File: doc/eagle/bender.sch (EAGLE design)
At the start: 11 parts

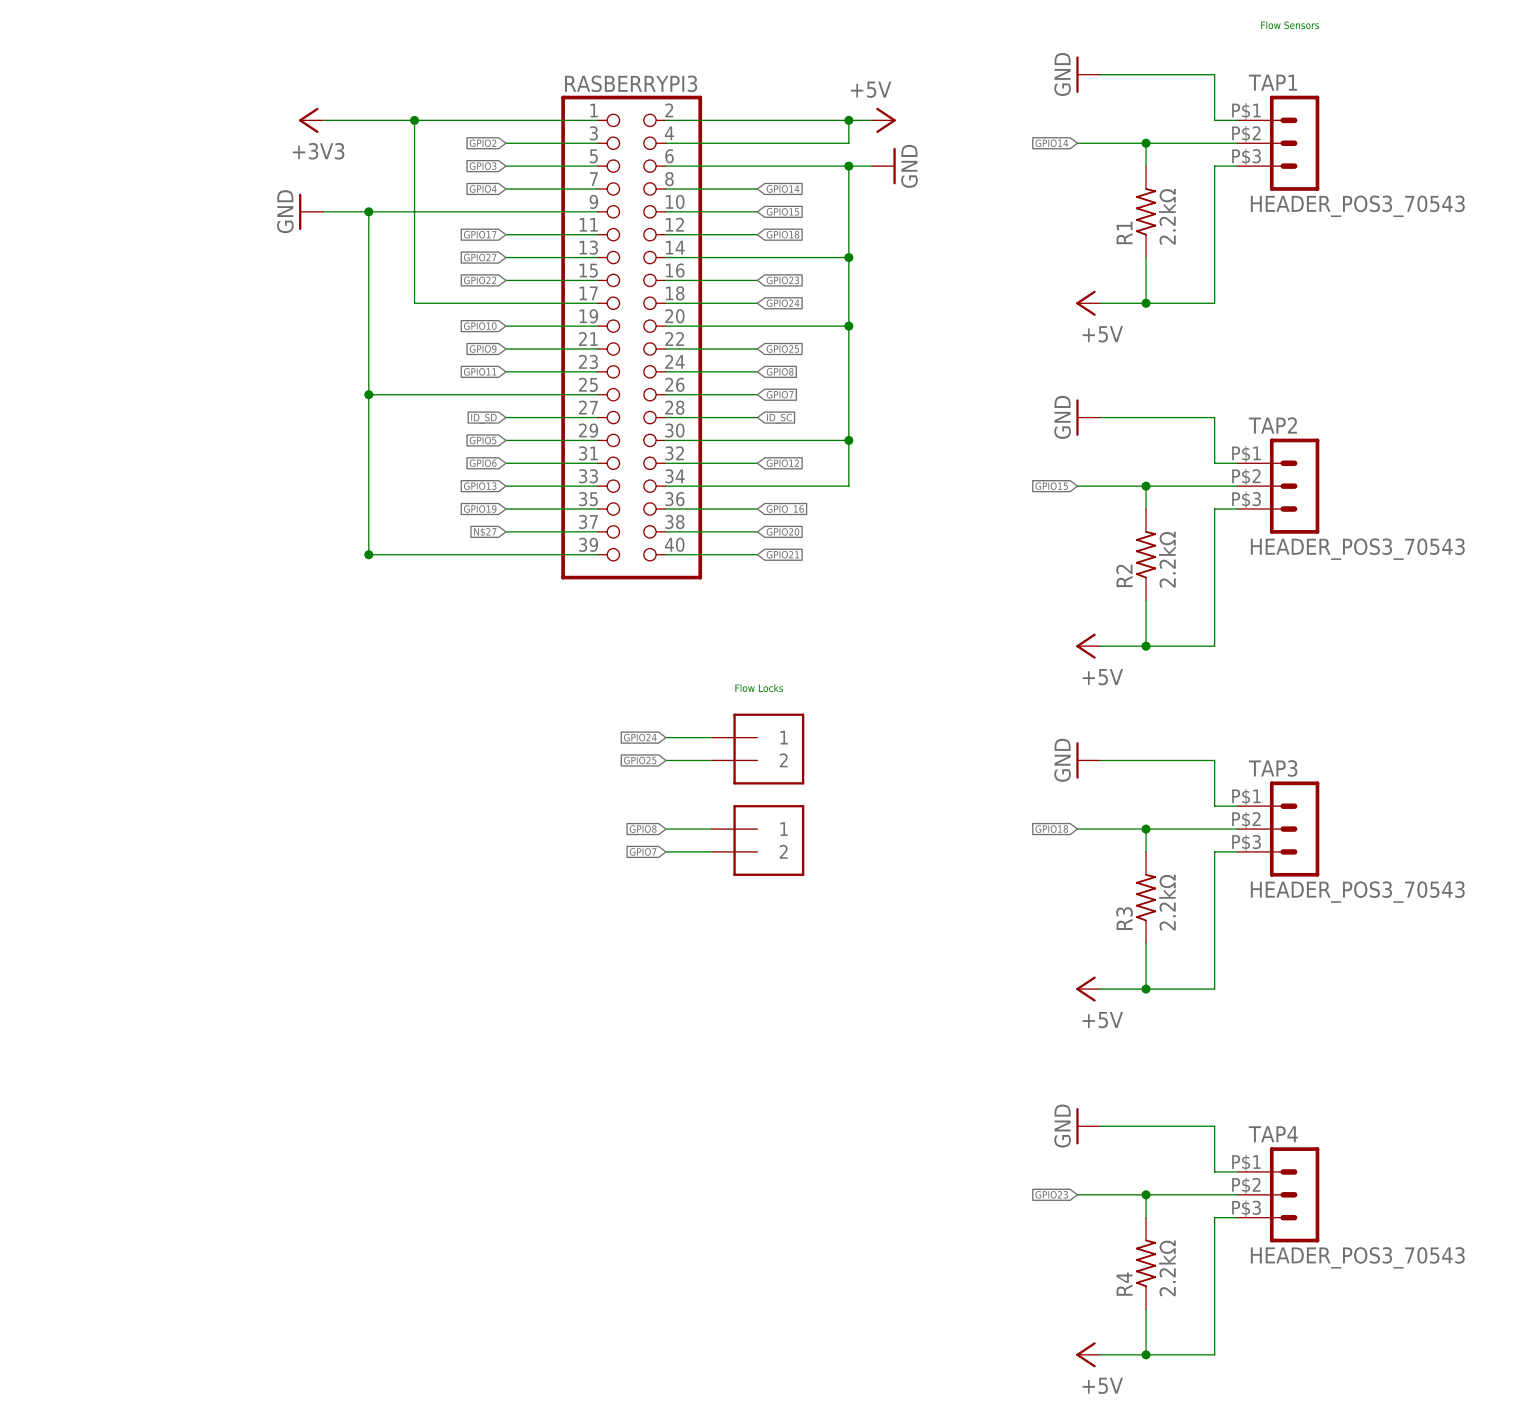
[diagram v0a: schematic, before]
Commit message: Update schematics to use 3v3 for Pi inputs.
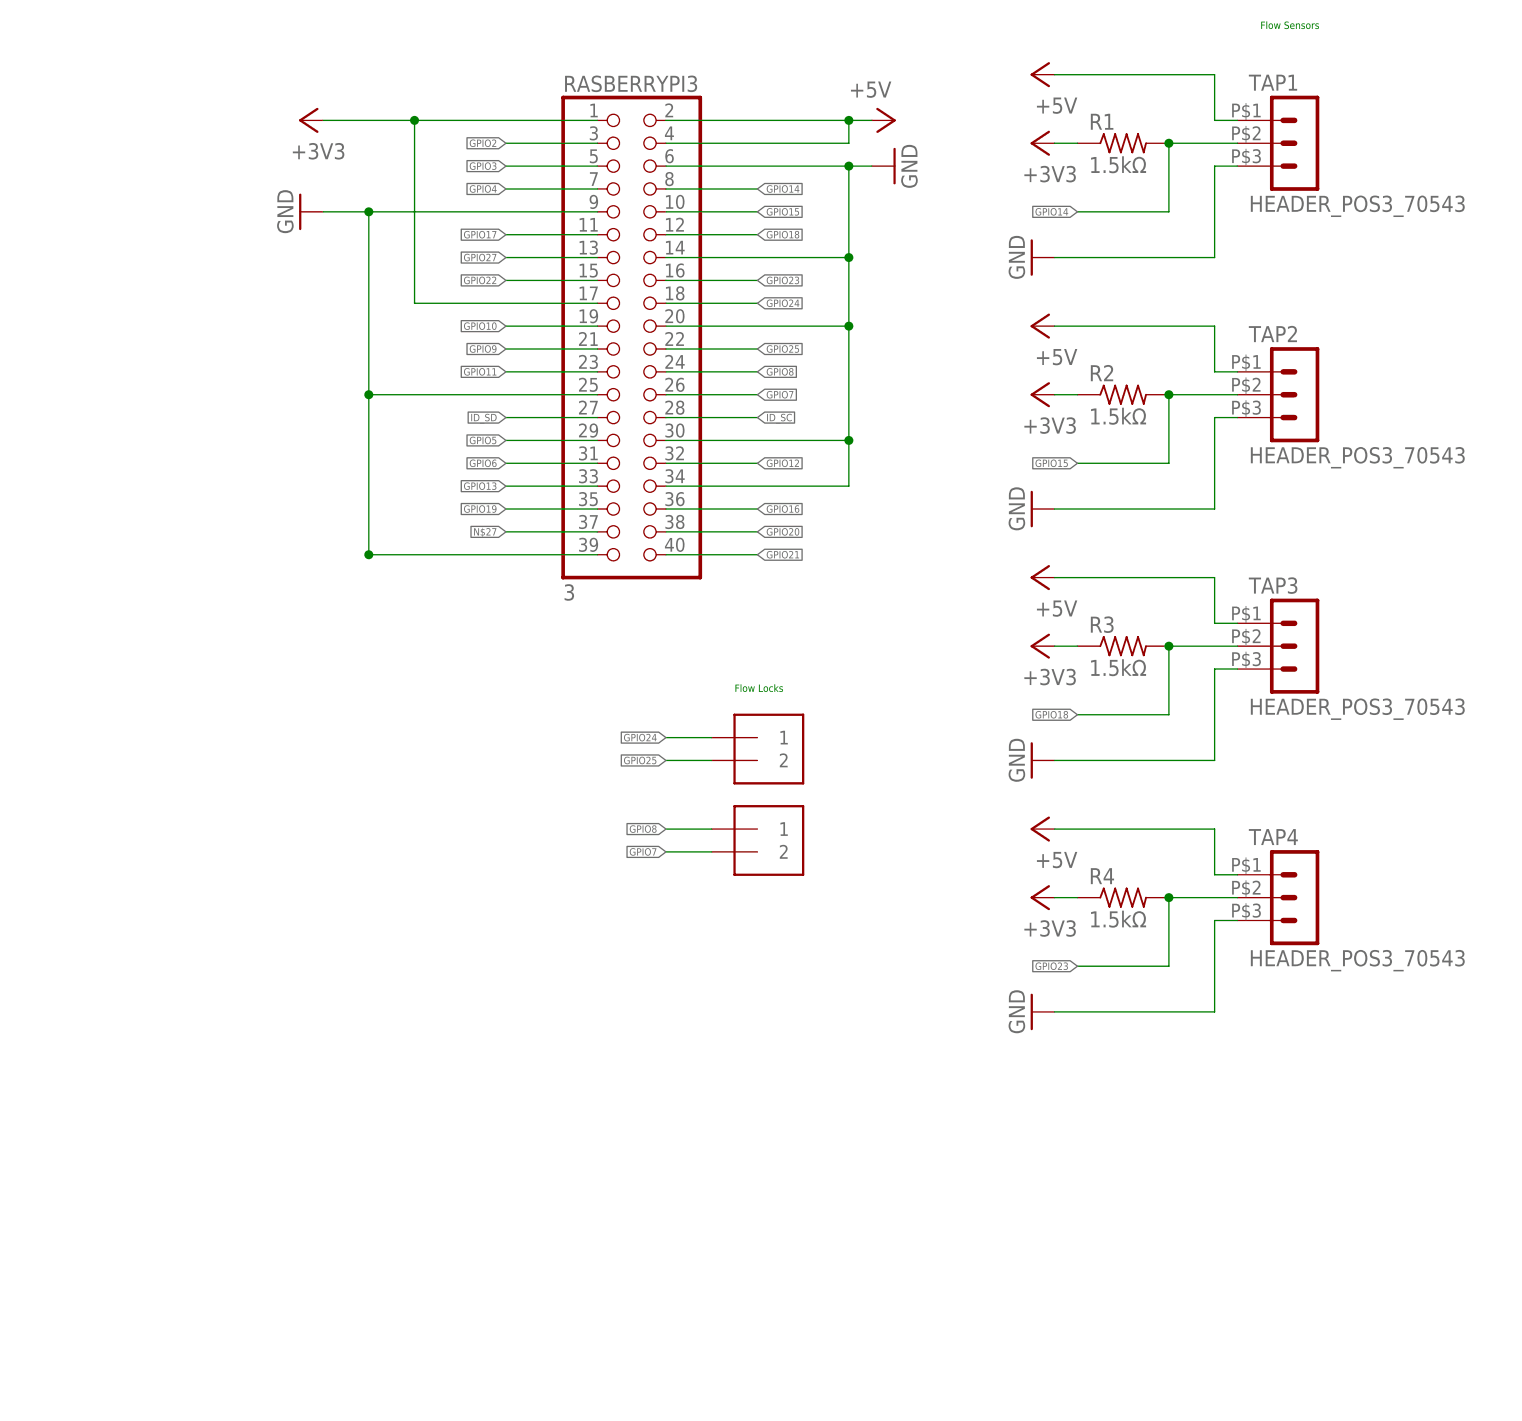
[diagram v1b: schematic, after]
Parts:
- R1, R2, R3, R4: value 2.2kΩ -> 1.5kΩ
- RASBERRYPI3: value (none) -> 3
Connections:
- net GPIO_16 renamed GPIO16
- net +3V3: now also R1.1, R2.1, R3.1, R4.1
- net +5V: now also TAP1.1, TAP2.1, TAP3.1, TAP4.1; no longer R1.1, R2.1, R3.1, R4.1, TAP1.3, TAP2.3, TAP3.3, TAP4.3
- net GND: now also TAP1.3, TAP2.3, TAP3.3, TAP4.3; no longer TAP1.1, TAP2.1, TAP3.1, TAP4.1
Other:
- moved on the sheet: R1, R2, R3, R4, TAP2, TAP3, TAP4

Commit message: Add temp sensor to bender schematic.
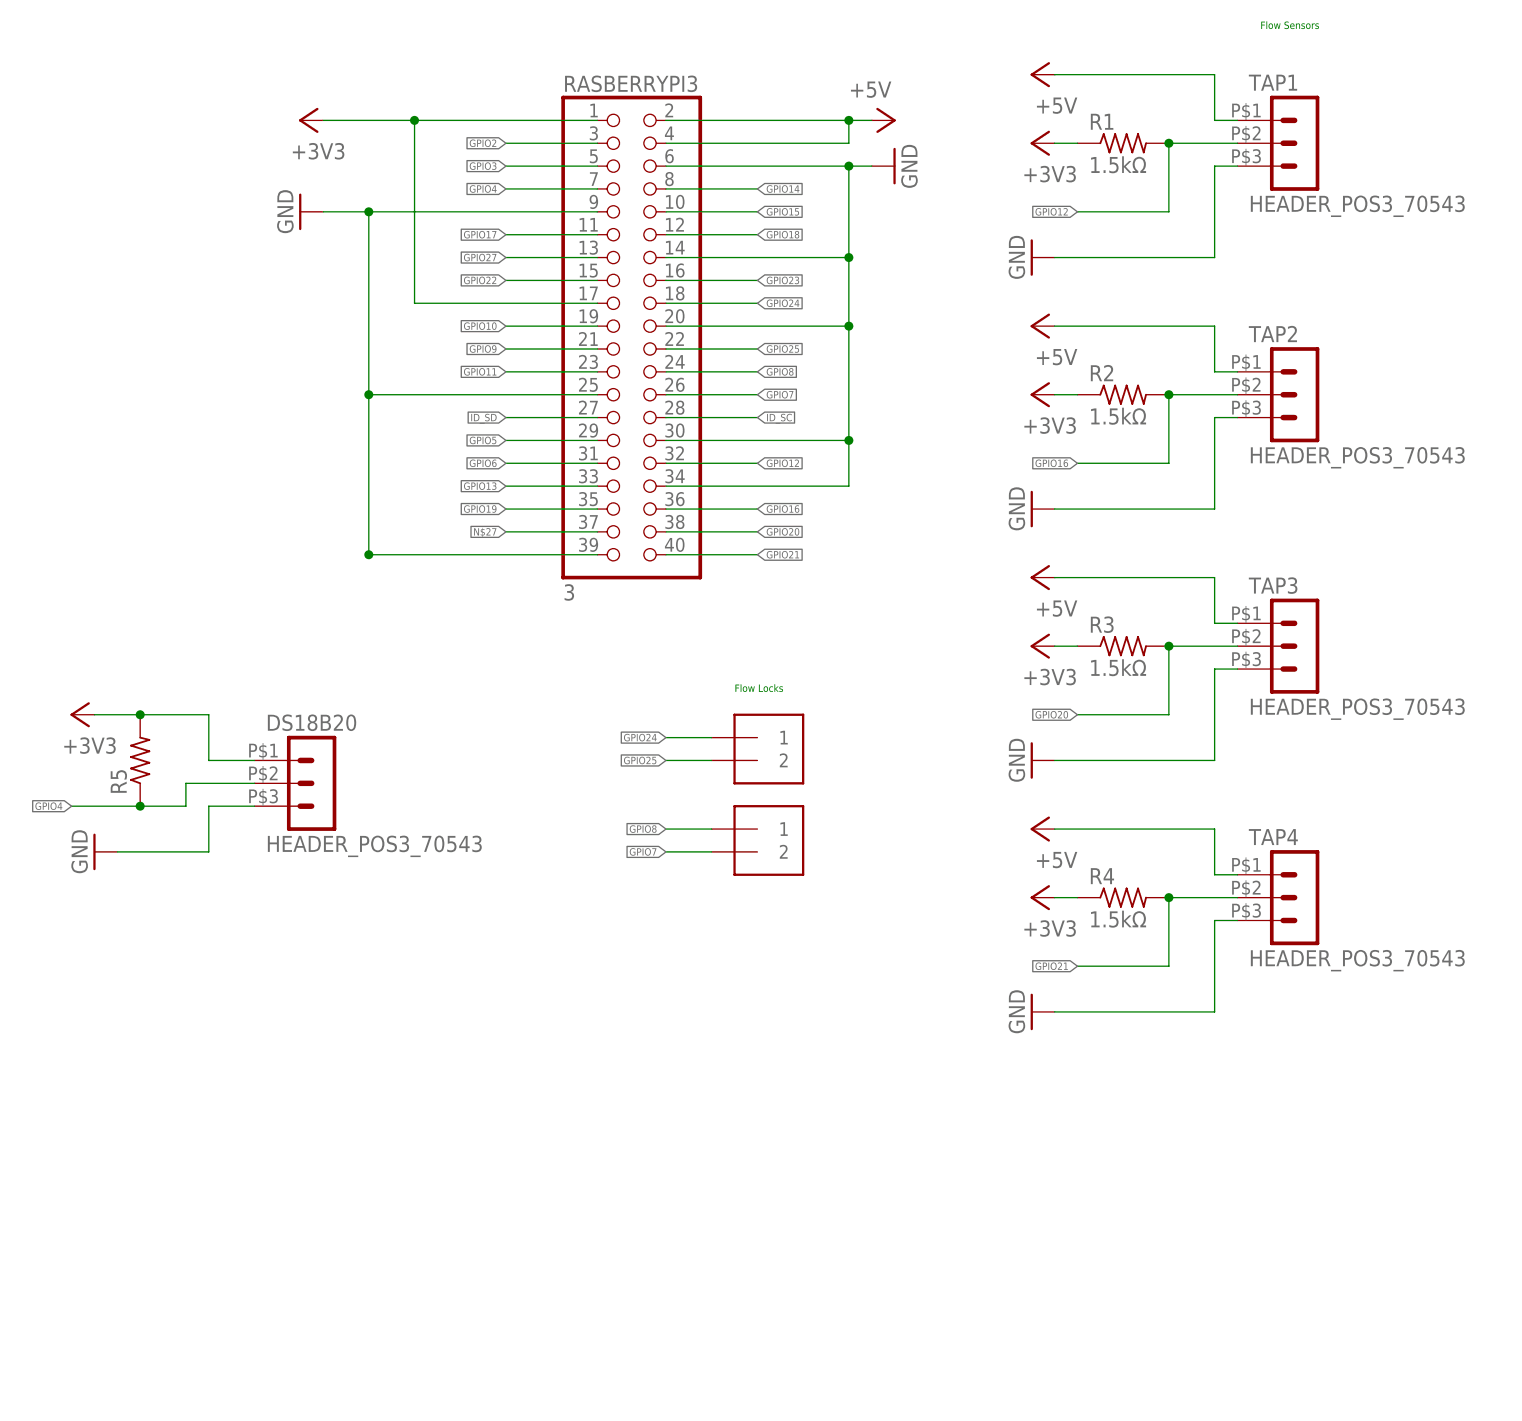
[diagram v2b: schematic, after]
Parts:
- added DS18B20: HEADER_POS3_70543, con-molex-c-grid-sl:HEADER_POS3_70543
- added R5: (no value), adafruit:R-US_0204/7
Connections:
- net +3V3: now also DS18B20.1, R5.2
- net GND: now also DS18B20.3
- net GPIO12: now also R1.2, TAP1.2
- net GPIO14: no longer R1.2, TAP1.2
- net GPIO15: no longer R2.2, TAP2.2
- net GPIO16: now also R2.2, TAP2.2
- net GPIO18: no longer R3.2, TAP3.2
- net GPIO20: now also R3.2, TAP3.2
- net GPIO21: now also R4.2, TAP4.2
- net GPIO23: no longer R4.2, TAP4.2
- net GPIO4: now also DS18B20.2, R5.1
